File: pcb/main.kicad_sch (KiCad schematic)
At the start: 7 parts, among them J6 SJ2-25773B-SMT-TR, SW2 SW_Push, U9 MAX6816

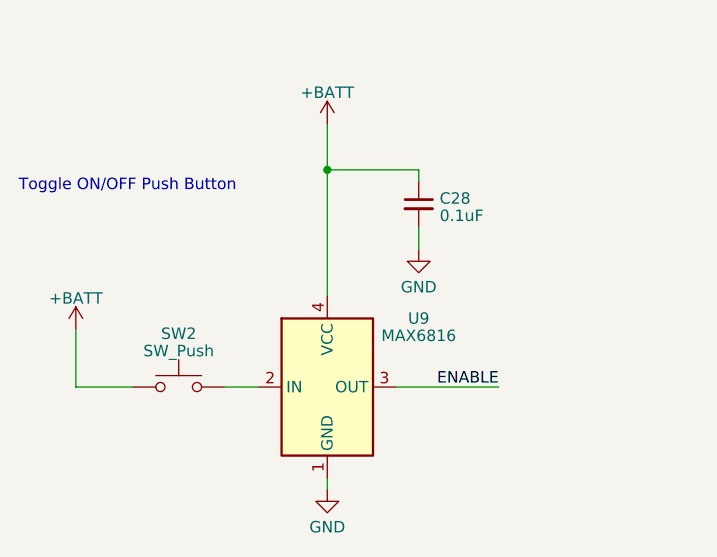
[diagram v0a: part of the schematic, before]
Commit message: Refactored details component namings + bom excludings
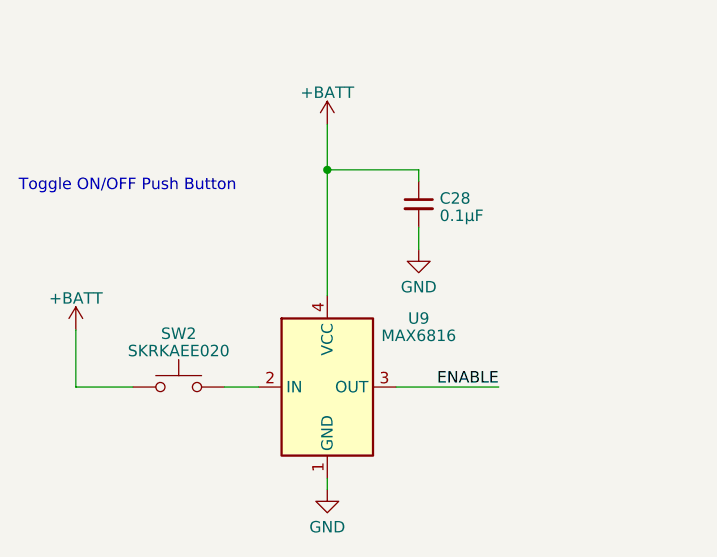
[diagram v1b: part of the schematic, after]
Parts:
- C28: value 0.1uF -> 0.1µF
- SW2: value SW_Push -> SKRKAEE020
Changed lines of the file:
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@@
       (effects (font (size 1.27 1.27)))
     )
-    (property "Value" "SW_Push" (at 45.72 163.6301 0)
+    (property "Value" "SKRKAEE020" (at 45.72 163.6301 0)
       (effects (font (size 1.27 1.27)))
     )
@@
       (effects (font (size 1.27 1.27)) (justify left))
     )
-    (property "Value" "0.1uF" (at 74.7141 148.6036 0)
+    (property "Value" "0.1µF" (at 74.7141 148.6036 0)
       (effects (font (size 1.27 1.27)) (justify left))
     )

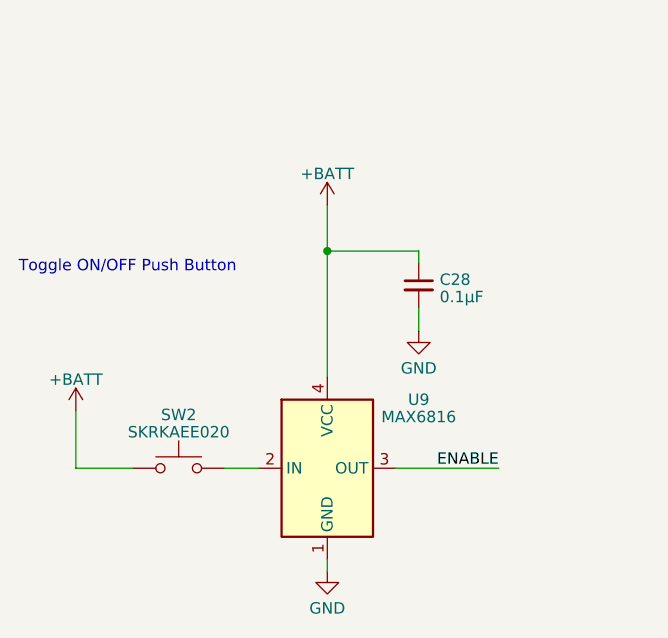
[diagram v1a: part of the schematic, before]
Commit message: Removed debounce IC and replaced with default on off switch
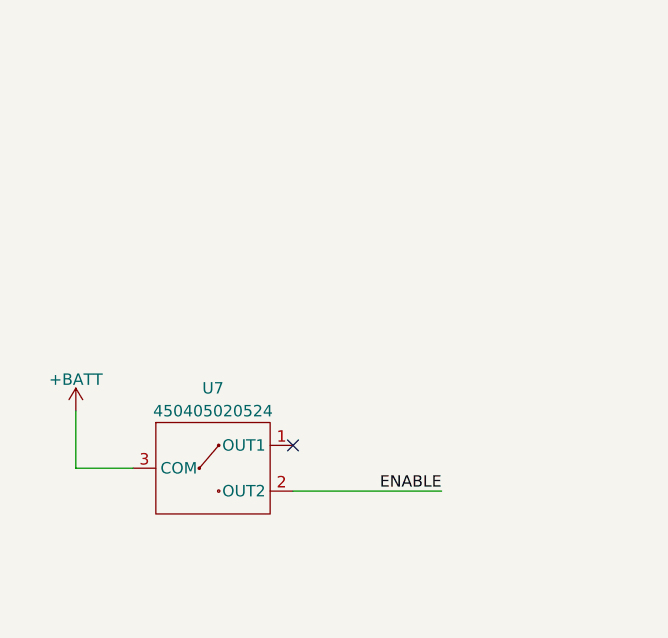
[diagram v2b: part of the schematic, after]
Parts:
- removed C28: 0.1µF, Capacitor_SMD:C_0603_1608Metric, symbol Device:C_Small
- removed SW2: SKRKAEE020, SKRKAEE020:SKRKAEE020, symbol Switch:SW_Push
- removed U9: MAX6816, Package_TO_SOT_SMD:SOT-143, symbol Interface:MAX6816
- added U7: 450405020524, 450405020524:450405020524, symbol 450405020524:450405020524
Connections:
- net +BATT: now also U7.3 (COM)
- net ENABLE: now also U7.2 (OUT2)
- no-connect marks 1 -> 2
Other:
- note removed: "Toggle ON/OFF Push Button"
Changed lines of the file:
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@@
 (kicad_sch (version 20230121) (generator eeschema)
   (paper "A4")
-  (junction (at 62.23 143.51) (diameter 0) (color 0 0 0 0)
-  )
   (junction (at 242.57 148.59) (diameter 0) (color 0 0 0 0)
   )
+  (no_connect (at 58.42 165.1))
   (no_connect (at 247.65 138.43))
   (wire (pts (xy 247.65 143.51) (xy 245.11 143.51))
@@
     (stroke (width 0) (type default))
   )
-  (wire (pts (xy 62.23 143.51) (xy 72.39 143.51))
-    (stroke (width 0) (type default))
-  )
-  (wire (pts (xy 72.39 149.86) (xy 72.39 152.4))
-    (stroke (width 0) (type default))
-  )
   (wire (pts (xy 62.23 72.39) (xy 76.2 72.39))
     (stroke (width 0) (type default))
@@
     (stroke (width 0) (type default))
   )
-  (wire (pts (xy 62.23 138.43) (xy 62.23 143.51))
-    (stroke (width 0) (type default))
-  )
-  (wire (pts (xy 50.8 167.64) (xy 54.61 167.64))
-    (stroke (width 0) (type default))
-  )
   (wire (pts (xy 57.15 60.96) (xy 76.2 60.96))
     (stroke (width 0) (type default))
@@
     (stroke (width 0) (type default))
   )
-  (wire (pts (xy 69.85 167.64) (xy 81.28 167.64))
+  (wire (pts (xy 58.42 170.18) (xy 74.93 170.18))
     (stroke (width 0) (type default))
   )
@@
     (stroke (width 0) (type default))
   )
-  (wire (pts (xy 62.23 177.8) (xy 62.23 179.07))
-    (stroke (width 0) (type default))
-  )
   (wire (pts (xy 57.15 58.42) (xy 76.2 58.42))
     (stroke (width 0) (type default))
@@
     (stroke (width 0) (type default))
   )
-  (wire (pts (xy 62.23 143.51) (xy 62.23 157.48))
-    (stroke (width 0) (type default))
-  )
   (wire (pts (xy 170.18 135.89) (xy 184.15 135.89))
-    (stroke (width 0) (type default))
-  )
-  (wire (pts (xy 72.39 144.78) (xy 72.39 143.51))
     (stroke (width 0) (type default))
   )
@@
     )
   )
-  (text "Toggle ON/OFF Push Button" (at 27.94 146.05 0)
-    (effects (font (size 1.27 1.27)) (justify left bottom))
-  )
   (label "USB_D-" (at 64.77 41.91 0) (fields_autoplaced)
     (effects (font (size 1.27 1.27)) (justify left bottom))
@@
     (effects (font (size 1.27 1.27)) (justify left bottom))
   )
-  (label "ENABLE" (at 81.28 167.64 180) (fields_autoplaced)
+  (label "ENABLE" (at 74.93 170.18 180) (fields_autoplaced)
     (effects (font (size 1.27 1.27)) (justify right bottom))
   )
@@
   (label "AUTOFOCUS" (at 62.23 74.93 0) (fields_autoplaced)
     (effects (font (size 1.27 1.27)) (justify left bottom))
-  )
-  (symbol (lib_id "Interface:MAX6816") (at 62.23 167.64 0) (unit 1)
-    (in_bom yes) (on_board yes) (dnp no)
-    (property "Reference" "U9" (at 72.39 160.02 0)
-      (effects (font (size 1.27 1.27)))
-    )
-    (property "Value" "MAX6816" (at 72.39 161.941 0)
-      (effects (font (size 1.27 1.27)))
-    )
-    (property "Footprint" "Package_TO_SOT_SMD:SOT-143" (at 78.74 179.07 0)
-      (effects (font (size 1.27 1.27)) hide)
-    )
-    (property "Datasheet" "https://datasheets.maximintegrated.com/en/ds/1896.pdf" (at 62.23 167.64 0)
-      (effects (font (size 1.27 1.27)) hide)
-    )
-    (pin "1")
-    (pin "2")
-    (pin "3")
-    (pin "4")
-    (instances
-      (project "rep-trap-pcb"
-        (path "/b363dc8f-4a45-4779-a397-ccb82393dab8"
-          (reference "U9") (unit 1)
-        )
-        (path "/b363dc8f-4a45-4779-a397-ccb82393dab8/eebb1d37-a01d-4adf-be70-a8e8f9293475"
-          (reference "U9") (unit 1)
-        )
-      )
-    )
   )
   (symbol (lib_id "Device:R_Small") (at 186.69 135.89 90) (unit 1)
@@
         (path "/b363dc8f-4a45-4779-a397-ccb82393dab8/eebb1d37-a01d-4adf-be70-a8e8f9293475"
           (reference "R23") (unit 1)
-        )
-      )
-    )
-  )
-  (symbol (lib_id "Switch:SW_Push") (at 45.72 167.64 0) (unit 1)
-    (in_bom yes) (on_board yes) (dnp no) (fields_autoplaced)
-    (property "Reference" "SW2" (at 45.72 161.7091 0)
-      (effects (font (size 1.27 1.27)))
-    )
-    (property "Value" "SKRKAEE020" (at 45.72 163.6301 0)
-      (effects (font (size 1.27 1.27)))
-    )
-    (property "Footprint" "SKRKAEE020:SKRKAEE020" (at 45.72 162.56 0)
-      (effects (font (size 1.27 1.27)) hide)
-    )
-    (property "Datasheet" "~" (at 45.72 162.56 0)
-      (effects (font (size 1.27 1.27)) hide)
-    )
-    (pin "1")
-    (pin "2")
-    (instances
-      (project "rep-trap-pcb"
-        (path "/b363dc8f-4a45-4779-a397-ccb82393dab8"
-          (reference "SW2") (unit 1)
-        )
-        (path "/b363dc8f-4a45-4779-a397-ccb82393dab8/eebb1d37-a01d-4adf-be70-a8e8f9293475"
-          (reference "SW2") (unit 1)
-        )
-      )
-    )
-  )
-  (symbol (lib_id "Device:C_Small") (at 72.39 147.32 0) (unit 1)
-    (in_bom yes) (on_board yes) (dnp no) (fields_autoplaced)
-    (property "Reference" "C28" (at 74.7141 146.6826 0)
-      (effects (font (size 1.27 1.27)) (justify left))
-    )
-    (property "Value" "0.1µF" (at 74.7141 148.6036 0)
-      (effects (font (size 1.27 1.27)) (justify left))
-    )
-    (property "Footprint" "Capacitor_SMD:C_0603_1608Metric" (at 72.39 147.32 0)
-      (effects (font (size 1.27 1.27)) hide)
-    )
-    (property "Datasheet" "~" (at 72.39 147.32 0)
-      (effects (font (size 1.27 1.27)) hide)
-    )
-    (pin "1")
-    (pin "2")
-    (instances
-      (project "rep-trap-pcb"
-        (path "/b363dc8f-4a45-4779-a397-ccb82393dab8"
-          (reference "C28") (unit 1)
-        )
-        (path "/b363dc8f-4a45-4779-a397-ccb82393dab8/eebb1d37-a01d-4adf-be70-a8e8f9293475"
-          (reference "C28") (unit 1)
         )
       )
@@
     )
   )
+  (symbol (lib_id "450405020524:450405020524") (at 49.53 167.64 0) (unit 1)
+    (in_bom yes) (on_board yes) (dnp no)
+    (property "Reference" "U7" (at 49.53 158.75 0)
+      (effects (font (size 1.27 1.27)))
+    )
+    (property "Value" "450405020524" (at 49.53 161.29 0)
+      (effects (font (size 1.27 1.27)))
+    )
+    (property "Footprint" "450405020524:450405020524" (at 49.53 167.64 0)
+      (effects (font (size 1.27 1.27)) hide)
+    )
+    (property "Datasheet" "" (at 49.53 167.64 0)
+      (effects (font (size 1.27 1.27)) hide)
+    )
+    (pin "1")
+    (pin "2")
+    (pin "3")
+    (instances
+      (project "rep-trap-pcb"
+        (path "/b363dc8f-4a45-4779-a397-ccb82393dab8/eebb1d37-a01d-4adf-be70-a8e8f9293475"
+          (reference "U7") (unit 1)
+        )
+      )
+    )
+  )
   (symbol (lib_id "power:+BATT") (at 34.29 161.29 0) (unit 1)
     (in_bom yes) (on_board yes) (dnp no) (fields_autoplaced)
@@
     )
   )
-  (symbol (lib_id "power:GND") (at 72.39 152.4 0) (unit 1)
-    (in_bom yes) (on_board yes) (dnp no) (fields_autoplaced)
-    (property "Reference" "#PWR067" (at 72.39 158.75 0)
-      (effects (font (size 1.27 1.27)) hide)
-    )
-    (property "Value" "GND" (at 72.39 156.5355 0)
-      (effects (font (size 1.27 1.27)))
-    )
-    (property "Footprint" "" (at 72.39 152.4 0)
-      (effects (font (size 1.27 1.27)) hide)
-    )
-    (property "Datasheet" "" (at 72.39 152.4 0)
-      (effects (font (size 1.27 1.27)) hide)
-    )
-    (pin "1")
-    (instances
-      (project "rep-trap-pcb"
-        (path "/b363dc8f-4a45-4779-a397-ccb82393dab8"
-          (reference "#PWR067") (unit 1)
-        )
-        (path "/b363dc8f-4a45-4779-a397-ccb82393dab8/eebb1d37-a01d-4adf-be70-a8e8f9293475"
-          (reference "#PWR072") (unit 1)
-        )
-      )
-    )
-  )
   (symbol (lib_id "power:GND") (at 191.77 149.86 0) (unit 1)
     (in_bom yes) (on_board yes) (dnp no) (fields_autoplaced)
@@
         (path "/b363dc8f-4a45-4779-a397-ccb82393dab8/eebb1d37-a01d-4adf-be70-a8e8f9293475"
           (reference "#PWR074") (unit 1)
-        )
-      )
-    )
-  )
-  (symbol (lib_id "power:GND") (at 62.23 179.07 0) (unit 1)
-    (in_bom yes) (on_board yes) (dnp no) (fields_autoplaced)
-    (property "Reference" "#PWR064" (at 62.23 185.42 0)
-      (effects (font (size 1.27 1.27)) hide)
-    )
-    (property "Value" "GND" (at 62.23 183.2055 0)
-      (effects (font (size 1.27 1.27)))
-    )
-    (property "Footprint" "" (at 62.23 179.07 0)
-      (effects (font (size 1.27 1.27)) hide)
-    )
-    (property "Datasheet" "" (at 62.23 179.07 0)
-      (effects (font (size 1.27 1.27)) hide)
-    )
-    (pin "1")
-    (instances
-      (project "rep-trap-pcb"
-        (path "/b363dc8f-4a45-4779-a397-ccb82393dab8"
-          (reference "#PWR064") (unit 1)
-        )
-        (path "/b363dc8f-4a45-4779-a397-ccb82393dab8/eebb1d37-a01d-4adf-be70-a8e8f9293475"
-          (reference "#PWR071") (unit 1)
         )
       )
@@
         )
       )
-    )
-  )
-  (symbol (lib_id "power:+BATT") (at 62.23 138.43 0) (unit 1)
-    (in_bom yes) (on_board yes) (dnp no) (fields_autoplaced)
-    (property "Reference" "#PWR066" (at 62.23 142.24 0)
-      (effects (font (size 1.27 1.27)) hide)
-    )
-    (property "Value" "+BATT" (at 62.23 134.9281 0)
-      (effects (font (size 1.27 1.27)))
-    )
-    (property "Footprint" "" (at 62.23 138.43 0)
-      (effects (font (size 1.27 1.27)) hide)
-    )
-    (property "Datasheet" "" (at 62.23 138.43 0)
-      (effects (font (size 1.27 1.27)) hide)
-    )
-    (pin "1")
-    (instances
-      (project "rep-trap-pcb"
-        (path "/b363dc8f-4a45-4779-a397-ccb82393dab8"
-          (reference "#PWR066") (unit 1)
-        )
-        (path "/b363dc8f-4a45-4779-a397-ccb82393dab8/eebb1d37-a01d-4adf-be70-a8e8f9293475"
-          (reference "#PWR070") (unit 1)
-        )
-      )

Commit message: Added notes and ToDos to be worked on for REV.02
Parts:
- removed R23, R24: 220, Resistor_SMD:R_0603_1608Metric, symbol Device:R_Small
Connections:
- net AUTOFOCUS: now also D5.3 (ANODE_2)
- net SHUTTER: now also D5.1 (ANODE_1)
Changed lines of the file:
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@@
-    (stroke (width 0) (type default))
-  )
-  (wire (pts (xy 189.23 135.89) (xy 194.31 135.89))
     (stroke (width 0) (type default))
   )
@@
     (stroke (width 0) (type default))
   )
-  (wire (pts (xy 170.18 144.78) (xy 184.15 144.78))
+  (wire (pts (xy 170.18 144.78) (xy 194.31 144.78))
     (stroke (width 0) (type default))
   )
@@
     (stroke (width 0) (type default))
   )
-  (wire (pts (xy 189.23 144.78) (xy 194.31 144.78))
-    (stroke (width 0) (type default))
-  )
   (wire (pts (xy 64.77 44.45) (xy 76.2 44.45))
     (stroke (width 0) (type default))
@@
     (stroke (width 0) (type default))
   )
-  (wire (pts (xy 170.18 135.89) (xy 184.15 135.89))
+  (wire (pts (xy 170.18 135.89) (xy 194.31 135.89))
     (stroke (width 0) (type default))
   )
@@
     (effects (font (size 1.27 1.27)) (justify left bottom))
   )
-  (symbol (lib_id "Device:R_Small") (at 186.69 135.89 90) (unit 1)
-    (in_bom yes) (on_board yes) (dnp no) (fields_autoplaced)
-    (property "Reference" "R23" (at 186.69 132.1435 90)
-      (effects (font (size 1.27 1.27)))
-    )
-    (property "Value" "220" (at 186.69 134.0645 90)
-      (effects (font (size 1.27 1.27)))
-    )
-    (property "Footprint" "Resistor_SMD:R_0603_1608Metric" (at 186.69 135.89 0)
-      (effects (font (size 1.27 1.27)) hide)
-    )
-    (property "Datasheet" "~" (at 186.69 135.89 0)
-      (effects (font (size 1.27 1.27)) hide)
-    )
-    (pin "1")
-    (pin "2")
-    (instances
-      (project "rep-trap-pcb"
-        (path "/b363dc8f-4a45-4779-a397-ccb82393dab8"
-          (reference "R23") (unit 1)
-        )
-        (path "/b363dc8f-4a45-4779-a397-ccb82393dab8/eebb1d37-a01d-4adf-be70-a8e8f9293475"
-          (reference "R23") (unit 1)
-        )
-      )
-    )
-  )
   (symbol (lib_id "ELD207:ELD207") (at 215.9 139.7 0) (unit 1)
     (in_bom yes) (on_board yes) (dnp no)
@@
         )
       )
-    )
-  )
-  (symbol (lib_id "Device:R_Small") (at 186.69 144.78 90) (unit 1)
-    (in_bom yes) (on_board yes) (dnp no) (fields_autoplaced)
-    (property "Reference" "R24" (at 186.69 141.0335 90)
-      (effects (font (size 1.27 1.27)))
-    )
-    (property "Value" "220" (at 186.69 142.9545 90)
-      (effects (font (size 1.27 1.27)))
-    )
-    (property "Footprint" "Resistor_SMD:R_0603_1608Metric" (at 186.69 144.78 0)
-      (effects (font (size 1.27 1.27)) hide)
-    )
-    (property "Datasheet" "~" (at 186.69 144.78 0)
-      (effects (font (size 1.27 1.27)) hide)
-    )
-    (pin "1")
-    (pin "2")
-    (instances
-      (project "rep-trap-pcb"
-        (path "/b363dc8f-4a45-4779-a397-ccb82393dab8"
-          (reference "R24") (unit 1)
-        )
-        (path "/b363dc8f-4a45-4779-a397-ccb82393dab8/eebb1d37-a01d-4adf-be70-a8e8f9293475"
-          (reference "R24") (unit 1)
-        )
-      )
